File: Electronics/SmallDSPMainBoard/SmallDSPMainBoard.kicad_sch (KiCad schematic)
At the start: 66 parts, among them J1 Header, J10 Programming, J16 Header, J2 Header, J3 Header, J4 Header, J5 Header, J6 Header, J7 Header, J8 Header, J9 Header, Q1 NSS1C300ET4, SW1 TS-1187A-B-A-B, SW2 CJS-1201TB, U1 ADAU1463, U2 ADM811, U3 M95M01-R, Y1 830105957509

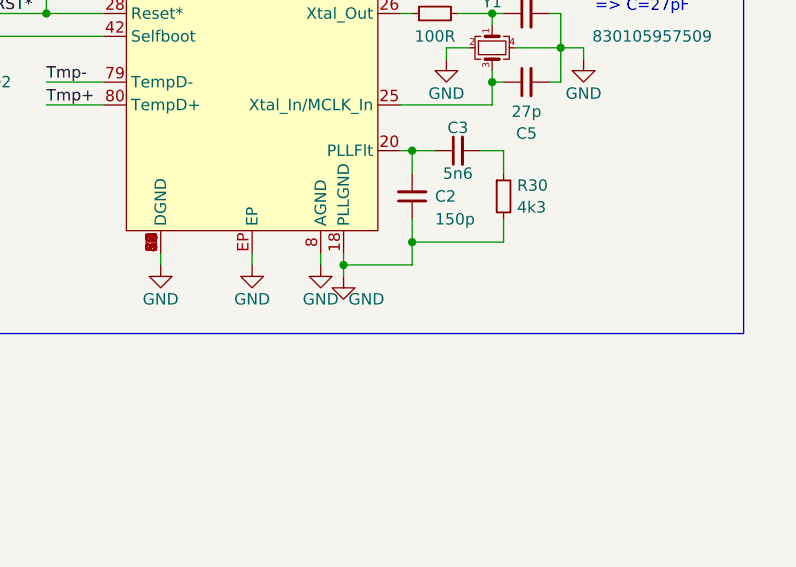
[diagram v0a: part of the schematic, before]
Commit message: Adds seperate ground for crystal and pll
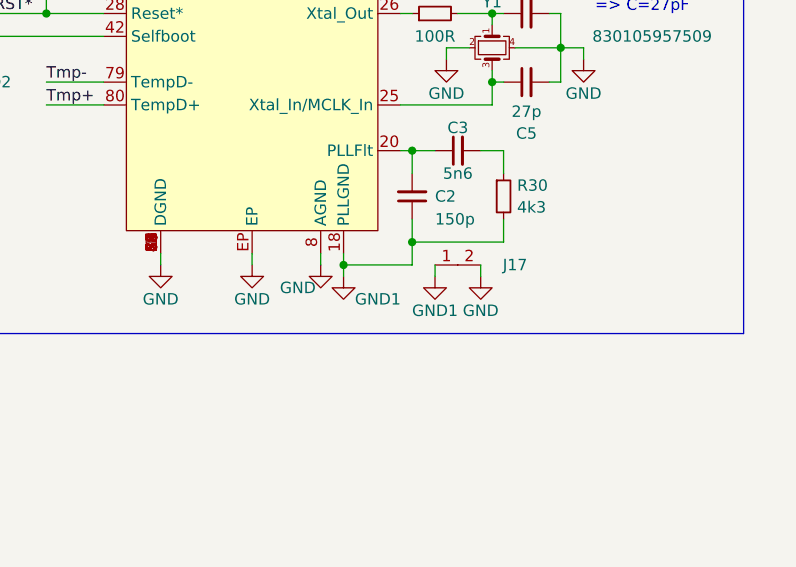
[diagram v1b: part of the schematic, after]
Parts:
- added J17: ~, 1_Project_Footprints:Short, symbol 1_Project_Symbols:Short
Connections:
- net GND: now also J17.2; no longer C2.1, R30.2, U1.18 (PLLGND)
- new net GND1: C2.1, J17.1, R30.2, U1.18 (PLLGND)
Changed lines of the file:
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@@
     (stroke (width 0) (type default))
   )
+  (wire (pts (xy 252.73 154.94) (xy 252.73 156.21))
+    (stroke (width 0) (type default))
+  )
   (wire (pts (xy 59.69 83.82) (xy 48.26 83.82))
     (stroke (width 0) (type default))
@@
     (stroke (width 0) (type default))
   )
+  (wire (pts (xy 247.65 154.94) (xy 247.65 156.21))
+    (stroke (width 0) (type default))
+  )
   (wire (pts (xy 25.4 184.15) (xy 33.02 184.15))
     (stroke (width 0) (type default))
@@
     )
   )
+  (symbol (lib_id "power:GND1") (at 237.49 156.21 0) (unit 1)
+    (in_bom yes) (on_board yes) (dnp no)
+    (property "Reference" "#PWR0219" (at 237.49 162.56 0)
+      (effects (font (size 1.27 1.27)) hide)
+    )
+    (property "Value" "GND1" (at 241.3 158.75 0)
+      (effects (font (size 1.27 1.27)))
+    )
+    (property "Footprint" "" (at 237.49 156.21 0)
+      (effects (font (size 1.27 1.27)) hide)
+    )
+    (property "Datasheet" "" (at 237.49 156.21 0)
+      (effects (font (size 1.27 1.27)) hide)
+    )
+    (pin "1")
+    (instances
+      (project "SmallDSPMainBoard"
+        (path "/5f2729b5-edcd-4fbc-b3fb-44096724c941"
+          (reference "#PWR0219") (unit 1)
+        )
+      )
+    )
+  )
   (symbol (lib_id "power:GND") (at 204.47 76.2 0) (unit 1)
     (in_bom yes) (on_board yes) (dnp no)
@@
       (effects (font (size 1.27 1.27)) hide)
     )
-    (property "Value" "GND" (at 234.95 158.75 0)
+    (property "Value" "GND" (at 232.41 157.48 0)
       (effects (font (size 1.27 1.27)))
     )
@@
     )
   )
-  (symbol (lib_id "power:GND") (at 237.49 156.21 0) (unit 1)
+  (symbol (lib_id "power:GND") (at 252.73 156.21 0) (unit 1)
     (in_bom yes) (on_board yes) (dnp no)
-    (property "Reference" "#PWR047" (at 237.49 162.56 0)
+    (property "Reference" "#PWR047" (at 252.73 162.56 0)
       (effects (font (size 1.27 1.27)) hide)
     )
-    (property "Value" "GND" (at 240.03 158.75 0)
+    (property "Value" "GND" (at 252.73 160.02 0)
       (effects (font (size 1.27 1.27)))
     )
-    (property "Footprint" "" (at 237.49 156.21 0)
+    (property "Footprint" "" (at 252.73 156.21 0)
       (effects (font (size 1.27 1.27)) hide)
     )
-    (property "Datasheet" "" (at 237.49 156.21 0)
+    (property "Datasheet" "" (at 252.73 156.21 0)
       (effects (font (size 1.27 1.27)) hide)
     )
@@
     )
   )
+  (symbol (lib_id "1_Project_Symbols:Short") (at 250.19 154.94 0) (unit 1)
+    (in_bom yes) (on_board yes) (dnp no)
+    (property "Reference" "J17" (at 256.54 154.94 0)
+      (effects (font (size 1.27 1.27)))
+    )
+    (property "Value" "~" (at 252.73 151.13 0)
+      (effects (font (size 1.27 1.27)))
+    )
+    (property "Footprint" "1_Project_Footprints:Short" (at 252.73 151.13 0)
+      (effects (font (size 1.27 1.27)) hide)
+    )
+    (property "Datasheet" "" (at 252.73 151.13 0)
+      (effects (font (size 1.27 1.27)) hide)
+    )
+    (pin "1")
+    (pin "2")
+    (instances
+      (project "SmallDSPMainBoard"
+        (path "/5f2729b5-edcd-4fbc-b3fb-44096724c941"
+          (reference "J17") (unit 1)
+        )
+      )
+    )
+  )
   (symbol (lib_id "Device:C_Small") (at 266.7 77.47 0) (unit 1)
     (in_bom yes) (on_board yes) (dnp no) (fields_autoplaced)
@@
         )
       )
+    )
+  )
+  (symbol (lib_id "power:GND1") (at 247.65 156.21 0) (unit 1)
+    (in_bom yes) (on_board yes) (dnp no)
+    (property "Reference" "#PWR0220" (at 247.65 162.56 0)
+      (effects (font (size 1.27 1.27)) hide)
+    )
+    (property "Value" "GND1" (at 247.65 160.02 0)
+      (effects (font (size 1.27 1.27)))
+    )
+    (property "Footprint" "" (at 247.65 156.21 0)
+      (effects (font (size 1.27 1.27)) hide)
+    )
+    (property "Datasheet" "" (at 247.65 156.21 0)
+      (effects (font (size 1.27 1.27)) hide)
+    )
+    (pin "1")
+    (instances
+      (project "SmallDSPMainBoard"
+        (path "/5f2729b5-edcd-4fbc-b3fb-44096724c941"
+          (reference "#PWR0220") (unit 1)
+        )
+      )

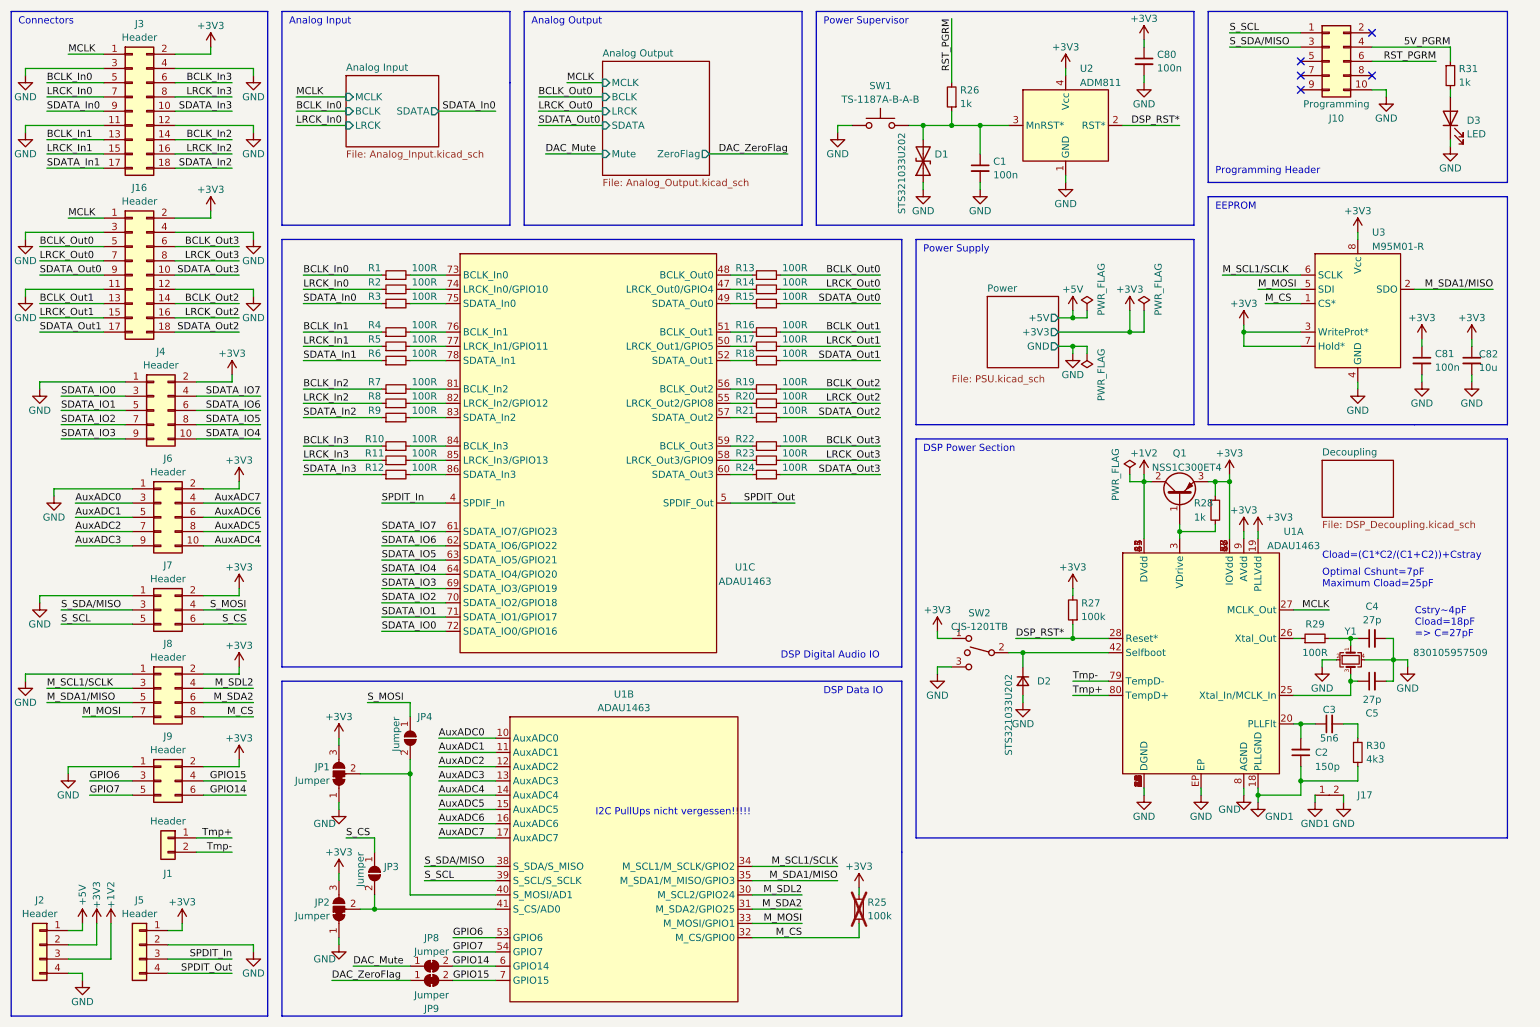
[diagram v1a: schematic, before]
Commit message: Partly finishes layout
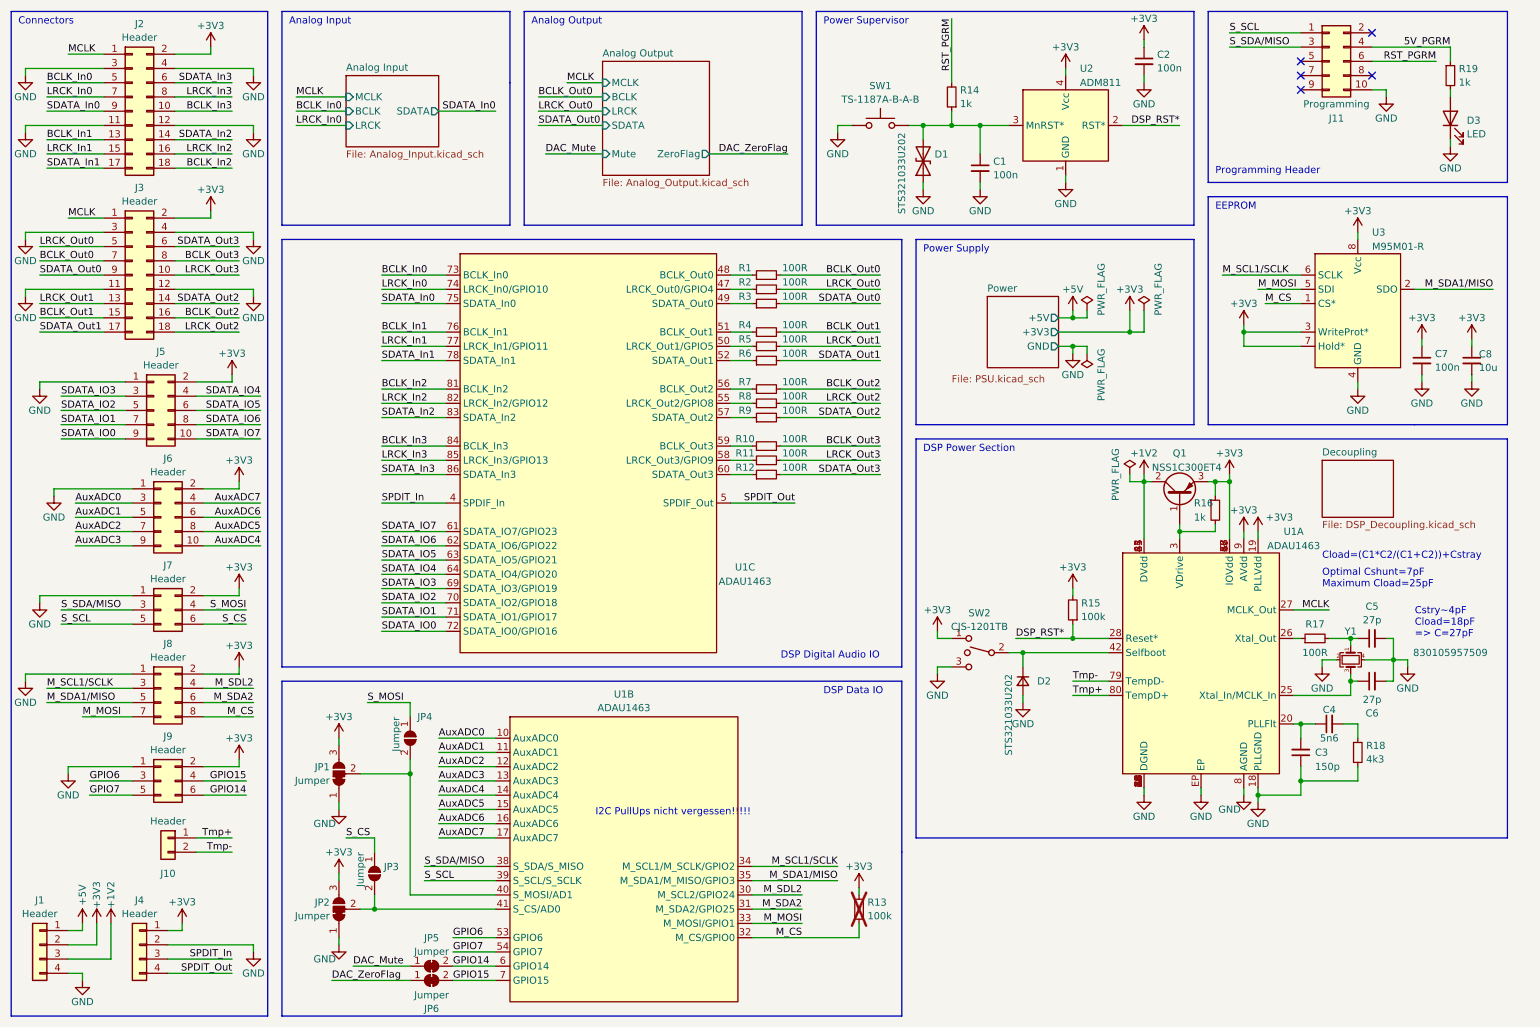
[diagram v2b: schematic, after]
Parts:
- removed J17: ~, 1_Project_Footprints:Short, symbol 1_Project_Symbols:Short
- removed R1, R10, R11, R12, R2, R3, R4, R5, R6, R7, R8, R9: 100R, Resistor_SMD:R_0402_1005Metric, symbol Device:R_Small
- renumbered C80 to C2, C2 to C3, C3 to C4, C4 to C5, C5 to C6, C81 to C7, C82 to C8, J2 to J1, J1 to J10, J10 to J11, J3 to J2, J16 to J3, J5 to J4, J4 to J5, JP8 to JP5, JP9 to JP6, R13 to R1, R22 to R10, R23 to R11, R24 to R12, R25 to R13, R26 to R14, R27 to R15, R28 to R16, R29 to R17, R30 to R18, R31 to R19, R14 to R2, R15 to R3, R16 to R4, R17 to R5, R18 to R6, R19 to R7, R20 to R8, R21 to R9
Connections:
- net GND1 is gone; now on net GND: C3.1, R18.2, U1.18 (PLLGND)
- net BCLK_In0: now also U1.73 (BCLK_In0)
- net BCLK_In1: now also U1.76 (BCLK_In1)
- net BCLK_In2: now also J2.18 (Pin_18), U1.81 (BCLK_In2); no longer J2.14 (Pin_14)
- net BCLK_In3: now also J2.10 (Pin_10), U1.84 (BCLK_In3); no longer J2.6 (Pin_6)
- net BCLK_Out0: now also J3.7 (Pin_7); no longer J3.5 (Pin_5)
- net BCLK_Out1: now also J3.15 (Pin_15); no longer J3.13 (Pin_13)
- net BCLK_Out2: now also J3.16 (Pin_16); no longer J3.14 (Pin_14)
- net BCLK_Out3: now also J3.8 (Pin_8); no longer J3.6 (Pin_6)
- net LRCK_In0: now also U1.74 (LRCK_In0/GPIO10)
- net LRCK_In1: now also U1.77 (LRCK_In1/GPIO11)
- net LRCK_In2: now also U1.82 (LRCK_In2/GPIO12)
- net LRCK_In3: now also U1.85 (LRCK_In3/GPIO13)
- net LRCK_Out0: now also J3.5 (Pin_5); no longer J3.7 (Pin_7)
- net LRCK_Out1: now also J3.13 (Pin_13); no longer J3.15 (Pin_15)
- net LRCK_Out2: now also J3.18 (Pin_18); no longer J3.16 (Pin_16)
- net LRCK_Out3: now also J3.10 (Pin_10); no longer J3.8 (Pin_8)
- net SDATA_IO0: now also J5.9 (Pin_9); no longer J5.3 (Pin_3)
- net SDATA_IO1: now also J5.7 (Pin_7); no longer J5.5 (Pin_5)
- net SDATA_IO2: now also J5.5 (Pin_5); no longer J5.7 (Pin_7)
- net SDATA_IO3: now also J5.3 (Pin_3); no longer J5.9 (Pin_9)
- net SDATA_IO4: now also J5.4 (Pin_4); no longer J5.10 (Pin_10)
- net SDATA_IO5: now also J5.6 (Pin_6); no longer J5.8 (Pin_8)
- net SDATA_IO6: now also J5.8 (Pin_8); no longer J5.6 (Pin_6)
- net SDATA_IO7: now also J5.10 (Pin_10); no longer J5.4 (Pin_4)
- net SDATA_In0: now also U1.75 (SDATA_In0)
- net SDATA_In1: now also U1.78 (SDATA_In1)
- net SDATA_In2: now also J2.14 (Pin_14), U1.83 (SDATA_In2); no longer J2.18 (Pin_18)
- net SDATA_In3: now also J2.6 (Pin_6), U1.86 (SDATA_In3); no longer J2.10 (Pin_10)
- net SDATA_Out2: now also J3.14 (Pin_14); no longer J3.18 (Pin_18)
- net SDATA_Out3: now also J3.6 (Pin_6); no longer J3.10 (Pin_10)

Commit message: Finishes layout of Rev 1.0 and fixes a polarity error in the schematic
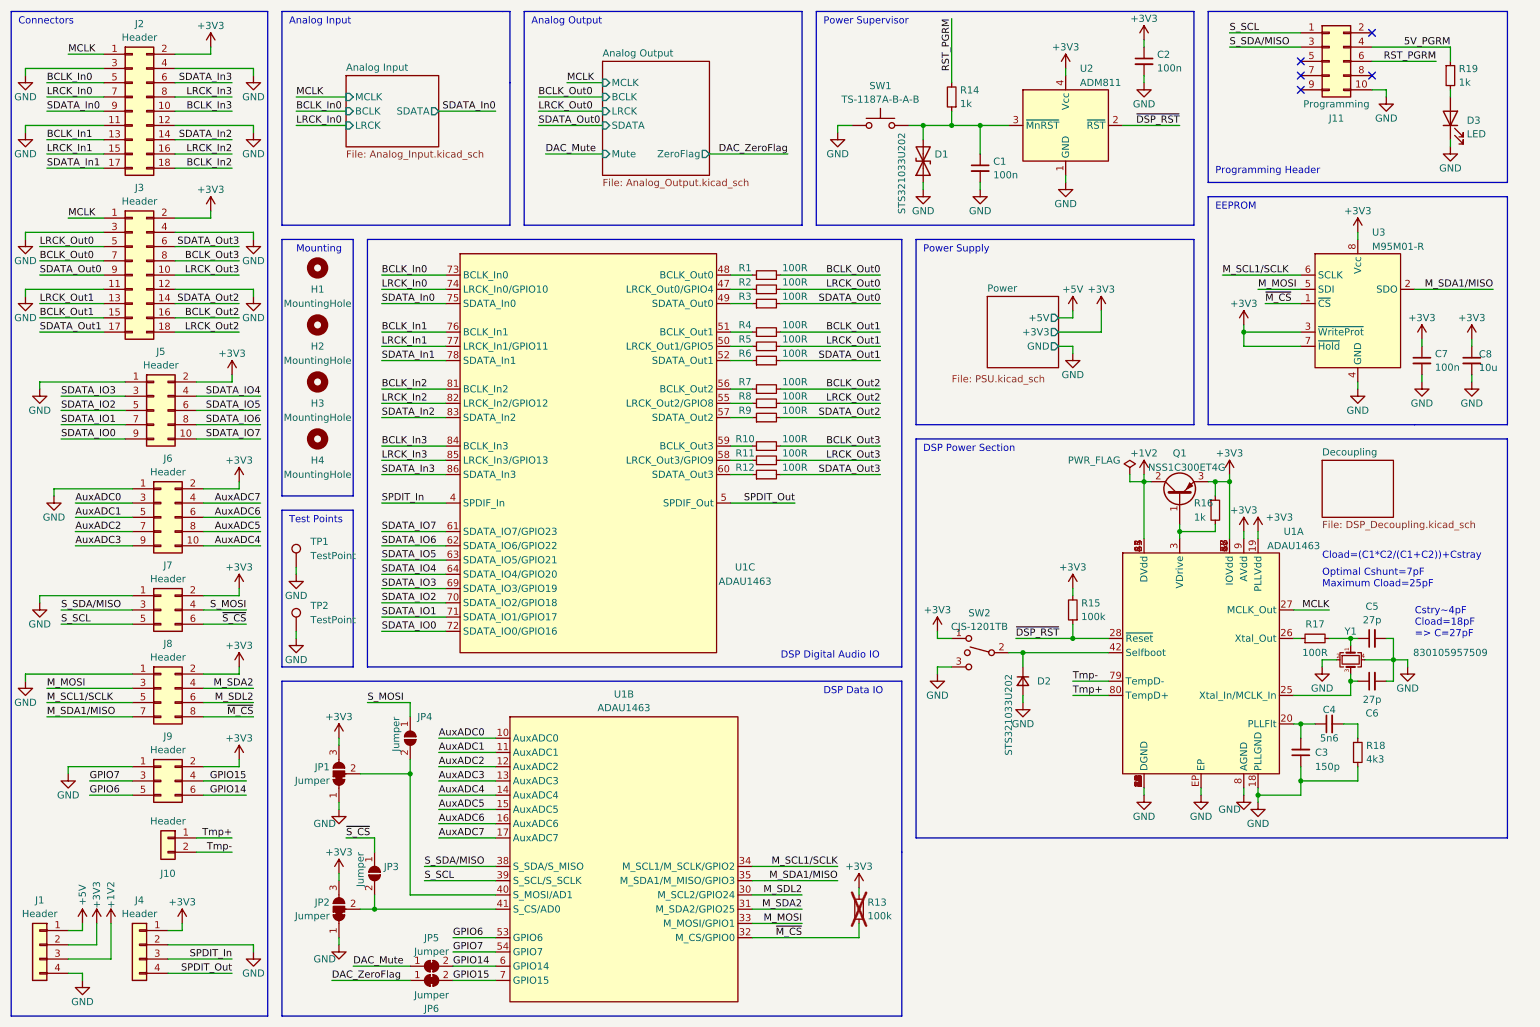
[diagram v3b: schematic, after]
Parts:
- added H1, H2, H3, H4: MountingHole, MountingHole:MountingHole_3.2mm_M3_ISO7380, symbol Mechanical:MountingHole
- added TP1, TP2: TestPoint, 1_Project_Footprints:TestPoint_Keystone_5019_Minature, symbol Connector:TestPoint
- J1, J10, J2, J3, J4, J5, J6, J7, J8, J9: Manufacturer (none) -> -; Part Number (none) -> -
- Q1: value NSS1C300ET4 -> NSS1C300ET4G; Part Number NSS1C300ET4 -> NSS1C300ET4G
- U1: Part Number ADAU1463 -> ADAU1463WBCPZ150
- U2: Part Number ADM811TARTZ -> ADM811TARTZ-REEL
- U3: Part Number M95M01-RMN -> M95M01-RMN6TP
- Y1: footprint Crystal:Crystal_SMD_3225-4Pin_3.2x2.5mm_HandSoldering -> Crystal:Crystal_SMD_3225-4Pin_3.2x2.5mm
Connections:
- net GND: now also TP1.1, TP2.1
- net GPIO6: now also J9.5 (Pin_5); no longer J9.3 (Pin_3)
- net GPIO7: now also J9.3 (Pin_3); no longer J9.5 (Pin_5)
- net M_MOSI: now also J8.3 (Pin_3); no longer J8.7 (Pin_7)
- net M_SCL1/SCLK: now also J8.5 (Pin_5); no longer J8.3 (Pin_3)
- net M_SDA1/MISO: now also J8.7 (Pin_7); no longer J8.5 (Pin_5)
- net M_SDA2: now also J8.4 (Pin_4); no longer J8.6 (Pin_6)
- net M_SDL2: now also J8.6 (Pin_6); no longer J8.4 (Pin_4)
- net DSP_RST* renamed ~{DSP_RST}
- net M_CS renamed ~{M_CS}
- net S_CS renamed ~{S_CS}
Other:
- note added: "Mounting"
- note added: "Test Points"
- note removed: "I2C PullUps nicht vergessen!!!!!"
